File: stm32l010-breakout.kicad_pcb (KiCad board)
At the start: 2 copper layers, 25.4 x 50.8 mm, 28 parts, among them J1 SWD, J2 Left, J3 Right, Q1 BC847BS, SW1 Reset, U1 STM32L010K8Tx, Y1 32.768kHz

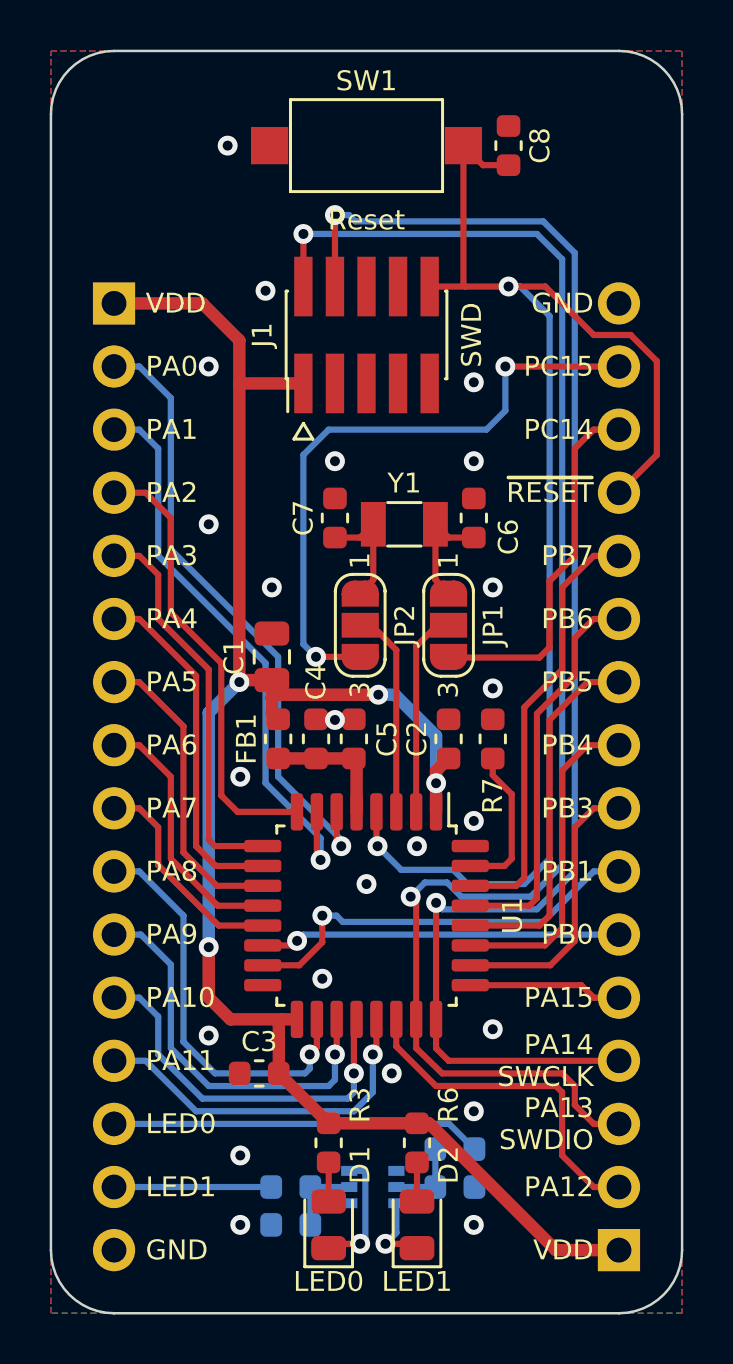
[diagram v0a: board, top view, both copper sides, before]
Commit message: Schematic cleanup, partial re-layout
- Changed the PCB size to 25x50mm
- Use 0R resistors for LSE oscillator/GPIO selection
- Schematic cleanup
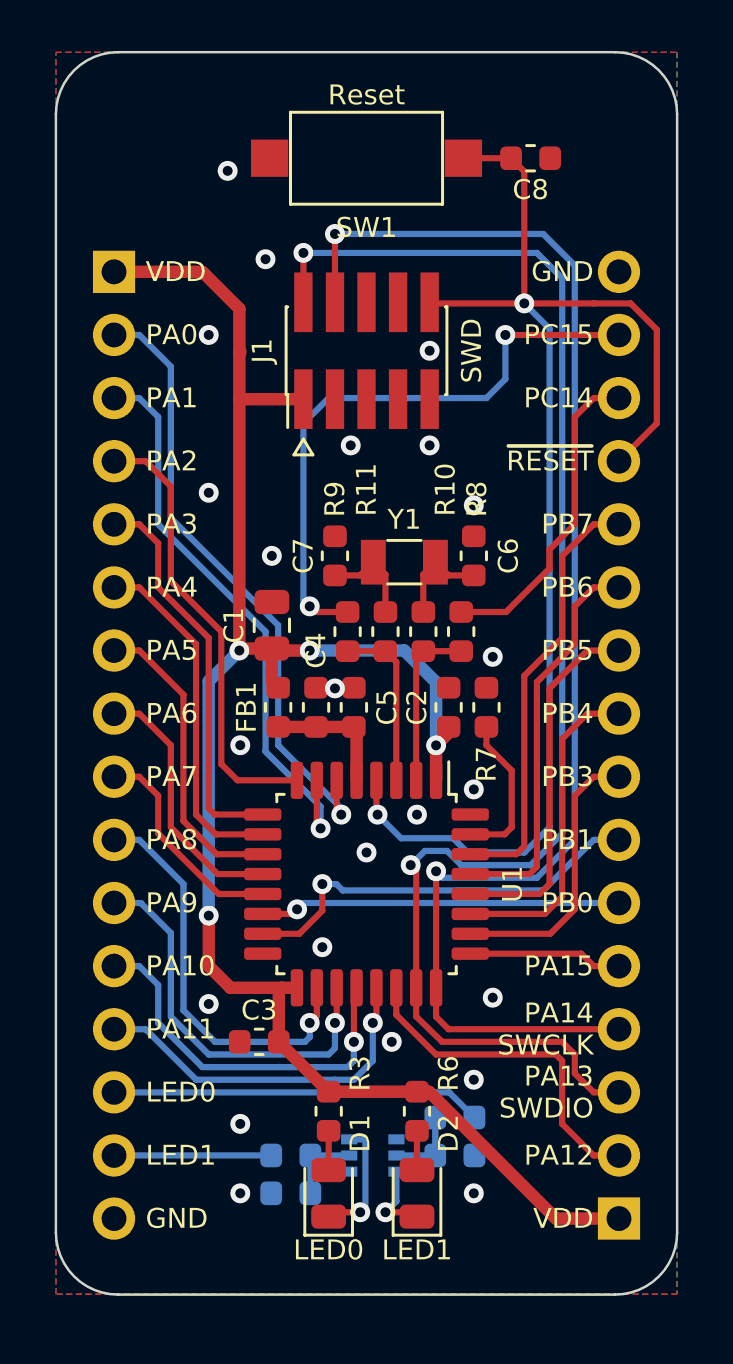
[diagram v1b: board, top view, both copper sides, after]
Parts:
- removed JP1: OSC32/PC14, Jumper:SolderJumper-3_P1.3mm_Open_RoundedPad1.0x1.5mm_NumberLabels
- removed JP2: OSC32/PC15, Jumper:SolderJumper-3_P1.3mm_Open_RoundedPad1.0x1.5mm_NumberLabels
- added R10: e, Resistor_SMD:R_0603_1608Metric, F.Cu at (129.3, 99.6)
- added R11: 0R, Resistor_SMD:R_0603_1608Metric, F.Cu at (127.8, 99.6)
- added R8: 0R, Resistor_SMD:R_0603_1608Metric, F.Cu at (130.8, 99.6)
- added R9: 0R, Resistor_SMD:R_0603_1608Metric, F.Cu at (126.2, 99.6)
- moved C6 1.52 mm to (131.3, 96.5)
- moved C7 1.52 mm to (125.7, 96.5)
- moved Y1 1.52 mm to (128.5, 96.8)
- moved R7 1.30 mm to (131.8, 102.6)
- moved C1 1.27 mm to (123.2, 99.3)
- moved U1 1.27 mm to (127.0, 109.7)
- moved #LOGO1 1.27 mm to (135.9, 80.0)
- moved C2 1.27 mm to (130.3, 102.6)
- moved C3 1.27 mm to (122.7, 116.1)
- moved C4 1.27 mm to (125.0, 102.6)
- moved C5 1.27 mm to (126.5, 102.6)
- moved D1 1.27 mm to (125.5, 122.2)
- moved D2 1.27 mm to (129.0, 122.2)
- moved FB1 1.27 mm to (123.4, 102.6)
- moved J2 1.27 mm to (116.8, 85.1)
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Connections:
- U1 pad 2: Net-(JP1-Pad2) -> /PC14_OSC32IN
- U1 pad 3: Net-(JP2-Pad2) -> /PC15_OSC32OUT
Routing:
- net Net-(JP2-Pad2): track 8.38 -> 0.00 mm
- net Net-(JP1-Pad2): track 8.32 -> 0.00 mm
- net /PC15_OSC32OUT: track 0.00 -> 6.90 mm
- net /PC14_OSC32IN: track 0.00 -> 6.84 mm
- net /~RESET: track 57.6 -> 54.4 mm
- net /PA13_SWDIO: track 60.5 -> 58.3 mm
- net /PA14_SWCLK: track 58.3 -> 56.3 mm
- net /PC14: track 14.7 -> 12.9 mm
- net /PC15: track 25.2 -> 24.2 mm
- net Net-(C7-Pad1): track 4.75 -> 3.97 mm
- net Net-(C6-Pad1): track 4.75 -> 3.97 mm
- net VDD: track 72.6 -> 73.1 mm
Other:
- board size 25.4 x 50.8 mm -> 25 x 50 mm
- board text added: "Rev. B"
- board text removed: "Rev. A"

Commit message: Finished laying out Revision B
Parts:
- Q1: value BC847BS -> BC847CDW1; moved to F.Cu
- R1, R2, R4, R5: moved to F.Cu
- R10: value e -> 0R
- moved R1 7.87 mm to (122.7, 119.1), turned to 180 degrees
- moved R2 5.06 mm to (125.7, 119.1)
- moved D1 3.59 mm to (129.0, 122.7)
- moved R3 3.59 mm to (129.0, 119.4)
- moved R4 3.30 mm to (122.7, 123.7)
- moved Q1 3.14 mm to (124.2, 121.4)
- moved D2 2.34 mm to (131.3, 122.7)
- moved R6 2.34 mm to (131.3, 119.4)
- moved R5 2.34 mm to (125.7, 123.7), turned to 180 degrees
- moved C6 2.18 mm to (130.0, 94.7), turned to 180 degrees
- moved C7 2.18 mm to (127.0, 94.7), turned to 0 degrees
- moved C3 0.25 mm to (122.7, 116.3)
- moved #LOGO1 0.13 mm to (135.8, 80.0)
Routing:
- net /LED0: track 14.9 -> 5.48 mm
- net /~RESET: track 54.4 -> 46.5 mm, vias 2 -> 3
- net Net-(D2-Pad1): track 3.16 -> 7.82 mm, vias 1 -> 0
- net Net-(D1-Pad1): track 4.97 -> 8.59 mm, vias 1 -> 2
- net Net-(Q1-Pad2): track 3.09 -> 4.49 mm
- net Net-(Q1-Pad5): track 3.09 -> 4.49 mm
- net /PC14: track 12.9 -> 14.0 mm, vias 0 -> 2
- net Net-(C7-Pad1): track 3.97 -> 5.06 mm
- net Net-(C6-Pad1): track 3.97 -> 5.06 mm
- net GND: vias 23 -> 24
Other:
- board size 25 x 50 mm -> 24 x 50 mm
- board text removed: "JP1, JP2 settings: 1-2: PC14,PC15 connected to the Y1 crystal 2-3: PC14,PC15 connected to the J3 header"
